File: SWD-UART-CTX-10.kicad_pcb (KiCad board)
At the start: 2 copper layers, 27.8 x 26.4 mm, 18 parts, among them J1 UE25BE5510H, J2 3020-10-0100-00, J3 SFH11-PBPC-D10-RA-BK, J4 Pins_2.54_1x2, U1 USBLC6-2P6, U2 FT230XQ

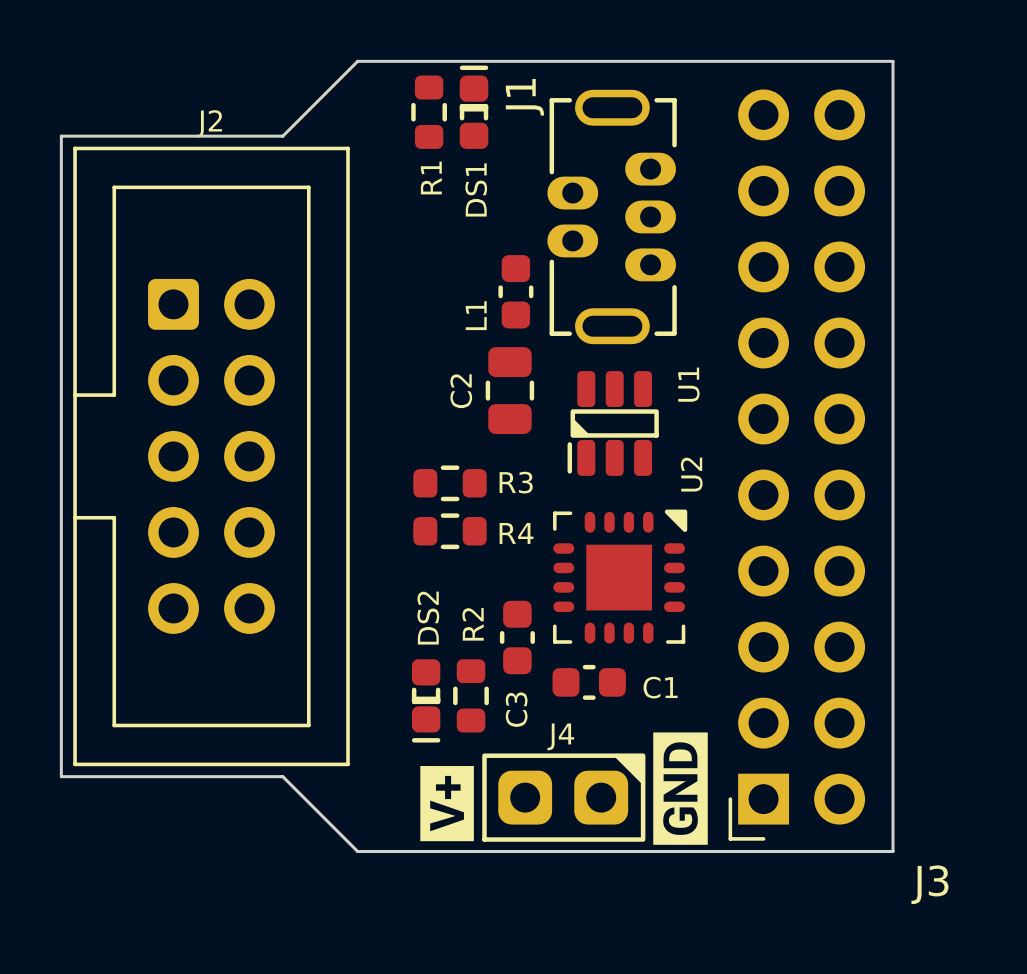
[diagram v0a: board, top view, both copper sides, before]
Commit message: Just use headers
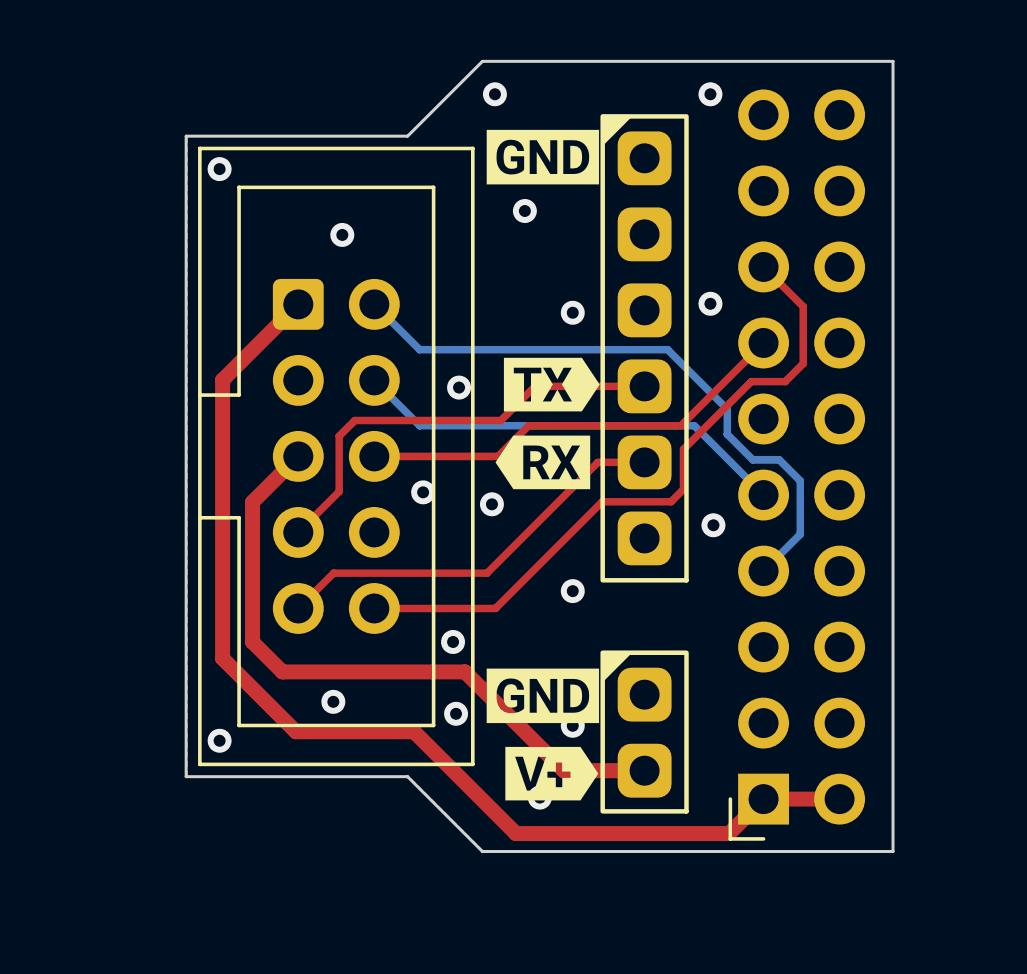
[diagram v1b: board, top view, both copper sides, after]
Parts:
- removed C1, C3: 100n, C_Capacitor:C_0603
- removed C2: 10u, C_Capacitor:C_0805
- removed DS1: LED_GRN, DS_LED:DS_0603
- removed DS2: LED_YEL, DS_LED:DS_0603
- removed L1: 600R, L_Inductor:FB_0603
- removed R1, R2, R3, R4: 470R, R_Resistor:R_0603
- removed U1: USBLC6-2P6, U_IC:SOT23_6
- removed U2: FT230XQ, U_IC:QFN16_065_4x4_EP
- removed kibuzzard-63788958: G***, kibuzzard-63788958
- removed kibuzzard-63788968: G***, kibuzzard-63788968
- added kibuzzard-637893A0: G***, kibuzzard-637893A0, F.Cu at (138.6, 90.8)
- added kibuzzard-637893BE: G***, kibuzzard-637893BE, F.Cu at (138.3, 93.4)
- added kibuzzard-637893D0: G***, kibuzzard-637893D0, F.Cu at (138.3, 83.2)
- added kibuzzard-637893D0: G***, kibuzzard-637893D0, F.Cu at (138.3, 101.2)
- added kibuzzard-637893E3: G***, kibuzzard-637893E3, F.Cu at (138.6, 103.8)
- J1: value UE25BE5510H -> Pins_2.54_1x6; footprint J_Connector:USB_Mini_TH_Vertical -> J_Connector:Pins-2.54-1x6
- moved J2 4.17 mm to (130.1, 88.1)
- moved J4 3.73 mm to (141.7, 101.2), turned to 0 degrees
- moved J1 2.25 mm to (141.7, 83.2), turned to 0 degrees
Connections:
- J1 pad 1: Net-(J1-Pad1) -> GND
- J1 pad 2: Net-(J1-Pad2) -> unconnected-(J1-Pad2)
- J1 pad 3: Net-(J1-Pad3) -> unconnected-(J1-Pad3)
- J1 pad 4: unconnected-(J1-Pad4) -> /TXD
- J1 pad 5: GND -> /RXD
- J1 pad 6: GND -> unconnected-(J1-Pad6)
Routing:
- net /TARGET_VCC: track 0.00 -> 36.4 mm
- net /RESET: track 0.00 -> 22.3 mm
- net /VAUX: track 0.00 -> 21.7 mm
- net /SWDIO: track 0.00 -> 20.7 mm
- net /TXD: track 0.00 -> 14.7 mm
- net /SWCLK: track 0.00 -> 14.6 mm
- net /SWO: track 0.00 -> 14.6 mm
- net /RXD: track 0.00 -> 13.6 mm
- net GND: vias 0 -> 18
- added copper zone on B.Cu, net GND
- added copper zone on F.Cu, net GND
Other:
- board size 27.8 x 26.4 mm -> 23.6 x 26.4 mm

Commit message: Add series R
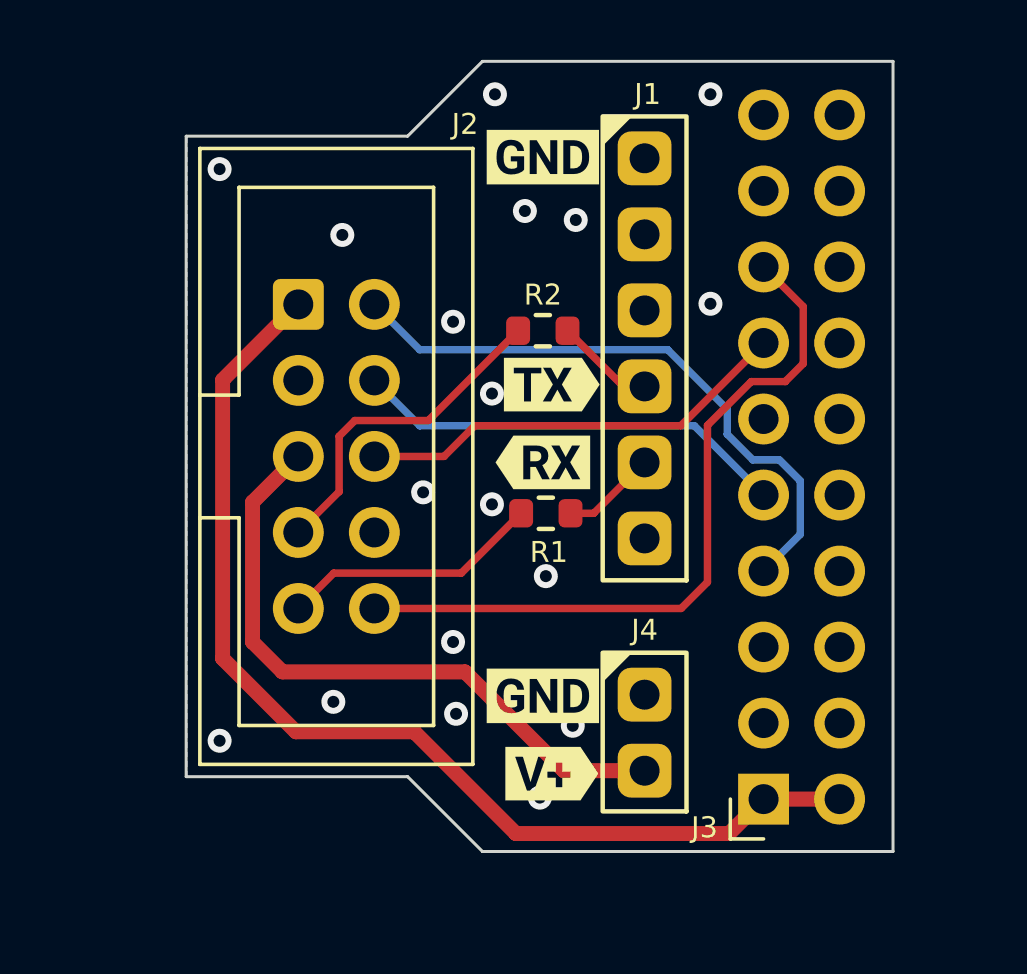
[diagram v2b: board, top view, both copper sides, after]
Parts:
- added R1: 470R, R_Resistor:R_0603, F.Cu at (138.4, 95.1)
- added R2: 470R, R_Resistor:R_0603, F.Cu at (138.3, 89.0)
- J1: value Pins_2.54_1x6 -> 61300611121
- J4: value Pins_2.54_1x2 -> 61300211121
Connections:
- J1 pad 4: /TXD -> Net-(J1-Pad4)
- J1 pad 5: /RXD -> Net-(J1-Pad5)
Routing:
- net /RXD: track 13.6 -> 8.76 mm
- net /TXD: track 14.7 -> 11.2 mm
- net Net-(J1-Pad4): track 0.00 -> 3.35 mm
- net Net-(J1-Pad5): track 0.00 -> 3.18 mm
- net /RESET: track 22.3 -> 24.6 mm

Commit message: Guild the lilly
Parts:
- added ~: TL_Embedded, N_NonPart:TL_Embedded_5mm, B.Cu at (137.7, 100.0)
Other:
- board text added: "SWD-UART-CTX-10 V1.0 Nov 22"

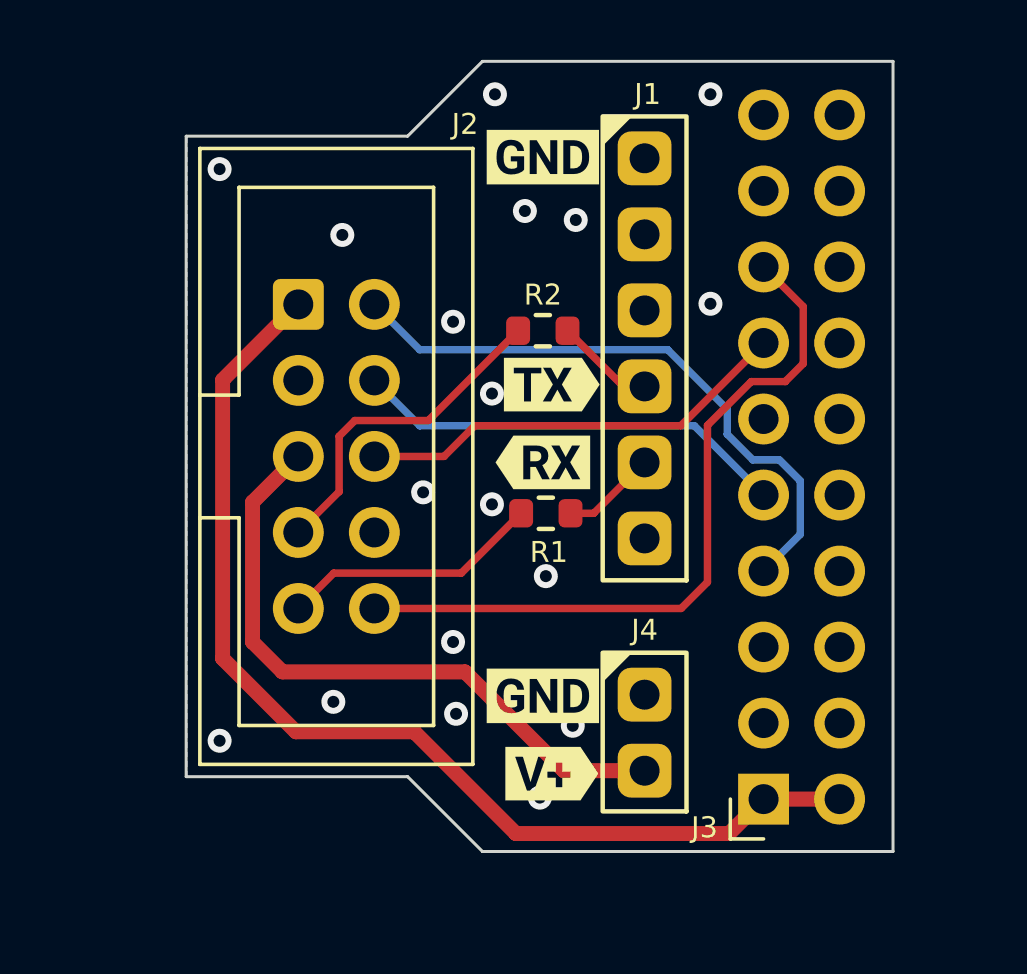
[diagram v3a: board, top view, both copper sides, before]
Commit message: Add jumper for vaux to vbus
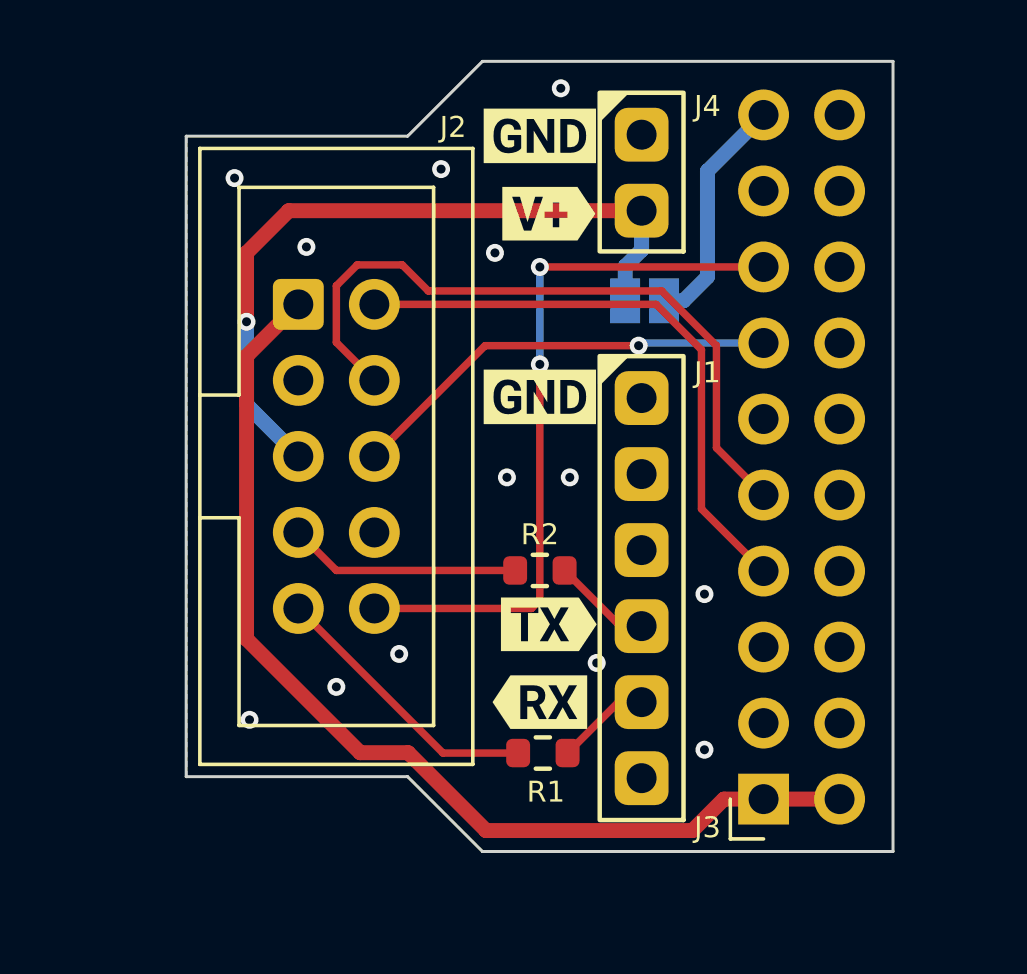
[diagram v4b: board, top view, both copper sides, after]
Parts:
- added JP1: SolderJumper_2_Open, Jumper:SolderJumper-2_P1.3mm_Open_Pad1.0x1.5mm, B.Cu at (141.7, 88.0)
- moved kibuzzard-637893D0 18.7 mm to (138.2, 82.5)
- moved J4 18.7 mm to (141.6, 82.5)
- moved kibuzzard-637893E3 18.7 mm to (138.5, 85.1)
- moved J1 8.01 mm to (141.6, 91.2)
- moved R1 8.01 mm to (138.3, 103.1)
- moved R2 8.01 mm to (138.2, 97.0)
- moved kibuzzard-637893A0 8.01 mm to (138.5, 98.8)
- moved kibuzzard-637893BE 8.01 mm to (138.2, 101.4)
- moved kibuzzard-637893D0 8.01 mm to (138.2, 91.2)
- moved ~ 1.13 mm to (136.9, 100.8)
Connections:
- J3 pad 19: unconnected-(J3-Pad19) -> Net-(J3-Pad19)
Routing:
- net /SWCLK: track 14.6 -> 23.4 mm
- net Net-(J3-Pad19): track 0.00 -> 7.97 mm
- net /TXD: track 11.2 -> 7.77 mm
- net /VAUX: track 21.7 -> 24.5 mm, vias 0 -> 1
- net /TARGET_VCC: track 36.4 -> 34.8 mm
- net /SWDIO: track 20.7 -> 19.8 mm
- net /RXD: track 8.76 -> 9.35 mm
- net /RESET: track 24.6 -> 24.3 mm, vias 0 -> 2
- net /SWO: vias 0 -> 1
- net GND: vias 18 -> 13
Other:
- board text added: "SWD-UART-CTX-10 V1.1 Nov 22"
- board text added: "VAUX-VBUS"
- board text removed: "SWD-UART-CTX-10 V1.0 Nov 22"
